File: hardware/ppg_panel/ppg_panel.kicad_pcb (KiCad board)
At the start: 2 copper layers, 70 x 80 mm, 60 parts

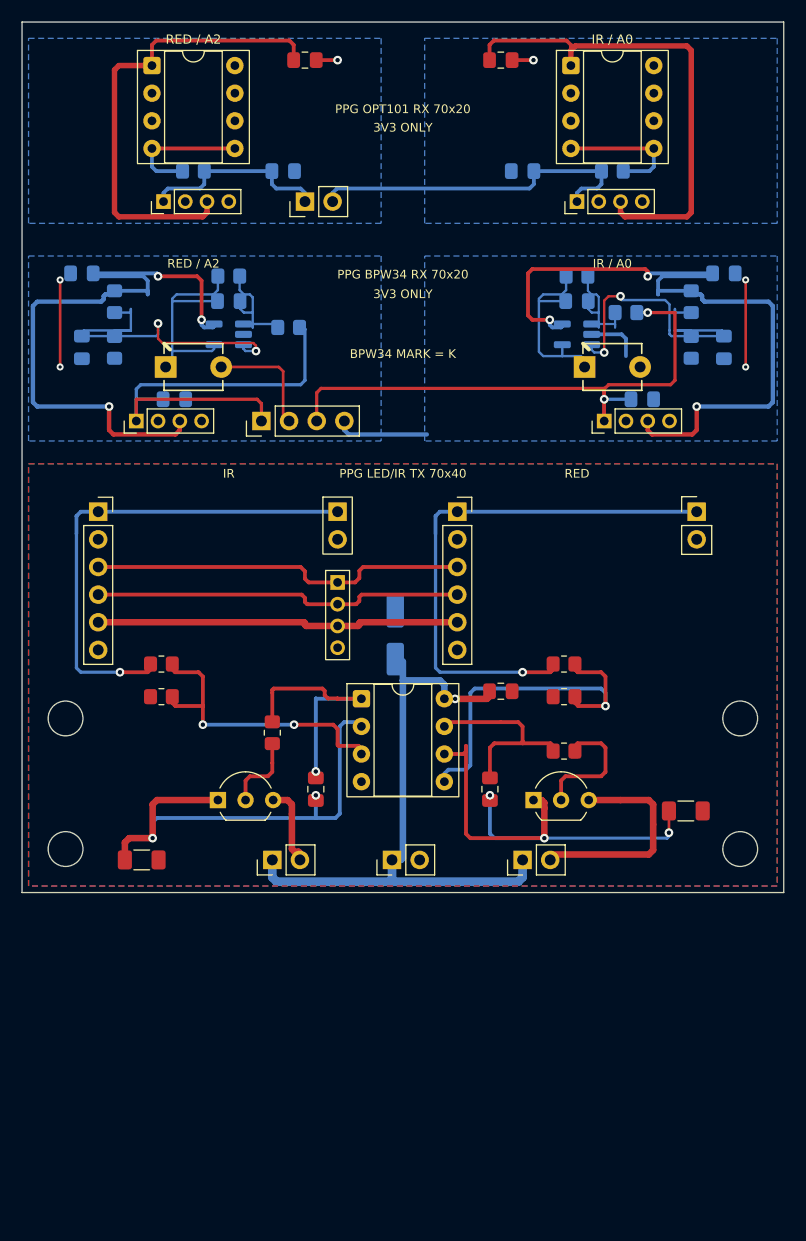
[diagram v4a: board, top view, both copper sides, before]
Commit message: Lengthen 45-degree PCB bends and refresh fabrication packages
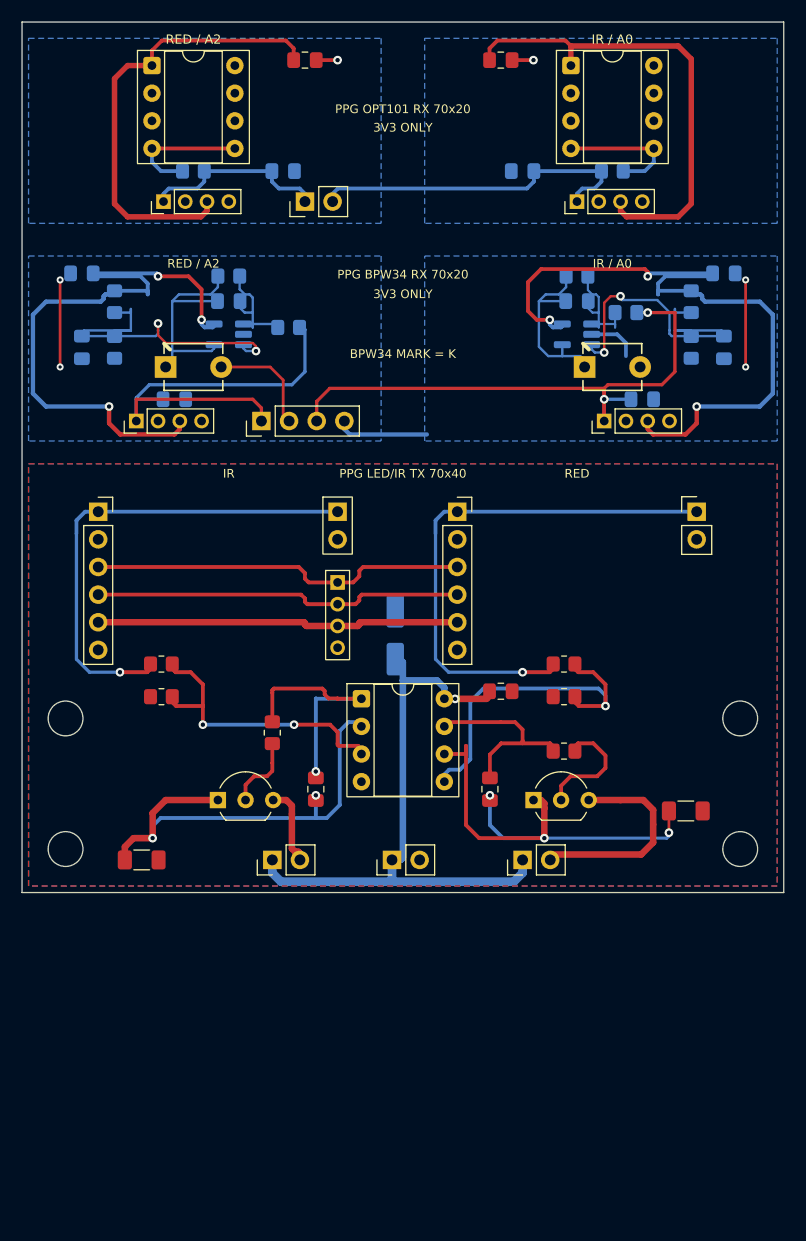
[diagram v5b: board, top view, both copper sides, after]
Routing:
- net BPW/3V3_IR: track 68.1 -> 65.8 mm
- net BPW/3V3_RED: track 60.2 -> 58.1 mm
- net TX/SENSE_IR: track 45.3 -> 43.7 mm
- net OPT/3V3_RED: track 43.2 -> 41.7 mm
- net TX/CMD_RED: track 33.8 -> 32.4 mm
- net BPW/OUT_RED: track 41.8 -> 40.6 mm
- net OPT/3V3_IR: track 46.6 -> 45.6 mm
- net TX/BASE_RED: track 12.0 -> 11.0 mm
- net BPW/OUT_IR: track 54.1 -> 53.2 mm
- net TX/SENSE_RED: track 45.4 -> 44.6 mm
- net TX/DAC_IR: track 45.7 -> 45.0 mm
- net TX/DAC_RED: track 49.7 -> 49.0 mm
- net TX/LED_K_RED: track 20.3 -> 19.6 mm
- net TX/5V: track 58.4 -> 57.7 mm
- net TX/CMD_IR: track 28.3 -> 27.6 mm
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
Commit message: Update README.md, hardware 45-degree routing and OPT101 diagnostic docs
- Fix version line in README.md to ensure version consistency test passes
- Document persistent live A0/A2 RX monitor dock and touch UI scaling
- Document OPT101 physical bench diagnostic protocol (docs/opt101-a0-diagnostic-2026-10-01.md)
- Detail 45-degree chamfered PCB routing, segment cleanup, and updated wiring guides
- Update repository tree and refreshed manufacturing release ZIPs
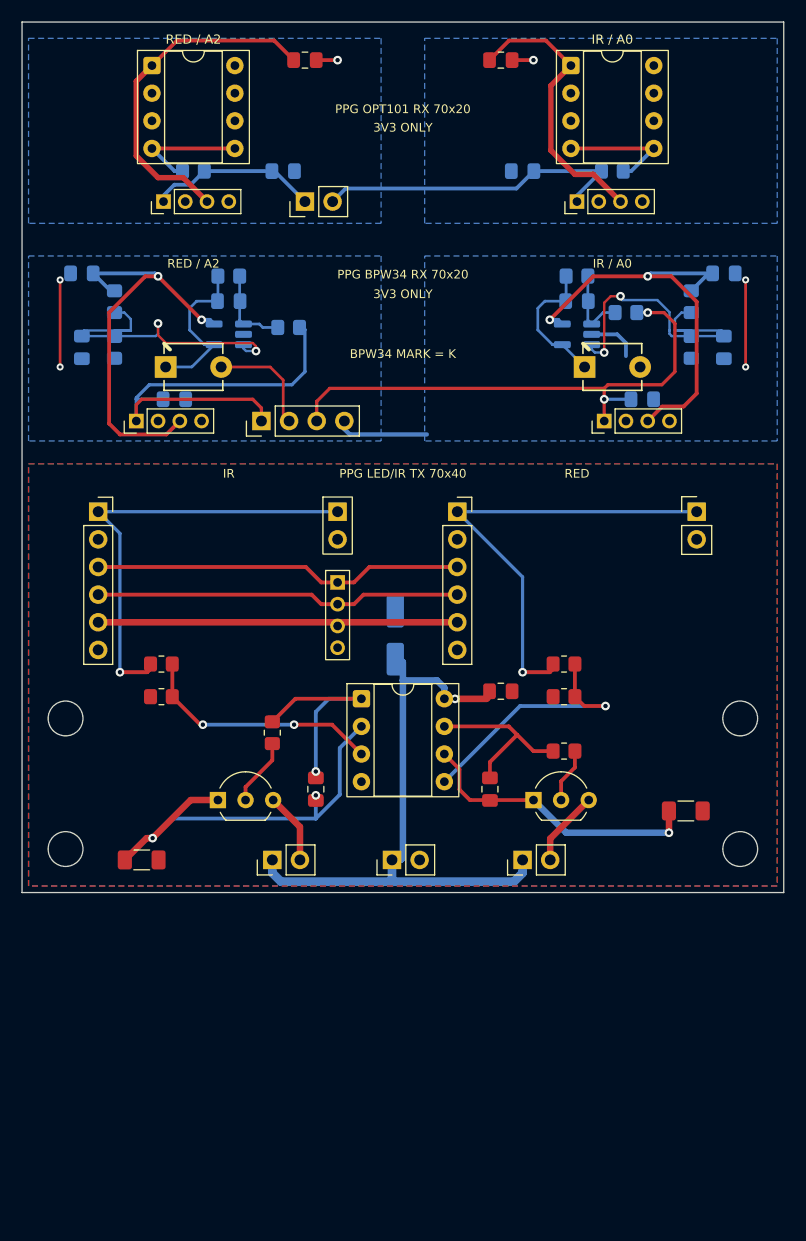
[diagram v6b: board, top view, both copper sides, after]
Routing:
- net BPW/3V3_IR: track 65.8 -> 39.8 mm, vias 3 -> 2
- net OPT/3V3_IR: track 45.6 -> 26.1 mm
- net BPW/3V3_RED: track 58.1 -> 39.2 mm, vias 3 -> 2
- net TX/SENSE_RED: track 44.6 -> 26.7 mm, vias 3 -> 1
- net TX/LED_K_RED: track 19.6 -> 6.97 mm
- net OPT/3V3_RED: track 41.7 -> 31.9 mm
- net TX/CMD_RED: track 32.4 -> 23.9 mm
- net TX/DAC_RED: track 49.0 -> 42.6 mm
- net TX/BASE_RED: track 11.0 -> 5.03 mm
- net BPW/SUM_RED: track 21.2 -> 15.2 mm
- net TX/CMD_IR: track 27.6 -> 22.6 mm
- net BPW/FB_IR: track 11.9 -> 7.13 mm
- net TX/SENSE_IR: track 43.7 -> 39.4 mm
- net BPW/SUM_IR: track 17.1 -> 12.8 mm
- net BPW/FB_RED: track 12.0 -> 7.83 mm
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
